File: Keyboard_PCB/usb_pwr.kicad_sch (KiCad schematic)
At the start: 57 parts, among them J2 USB-C 16P, U2 USBLC6-2SC6, U5 MCP73871, U6 MCP73871

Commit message: Battery charger layout done
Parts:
- removed C24: 22u, Capacitor_SMD:C_0603_1608Metric, symbol Device:C_Small
- removed C25: 100n, Capacitor_SMD:C_0603_1608Metric, symbol Device:C_Small
- removed C26, C27, C33, C34: 4u7, Capacitor_SMD:C_0603_1608Metric, symbol Device:C_Small
- removed C31, C32: 10u, Capacitor_SMD:C_0603_1608Metric, symbol Device:C_Small
- removed D5: PG, LED_SMD:LED_0603_1608Metric, symbol Device:LED_Small
- removed JP2: BAT_BYP, Jumper:SolderJumper-2_P1.3mm_Open_TrianglePad1.0x1.5mm, symbol Jumper:SolderJumper_2_Open
- removed R16, R17, R18, R19: 470, Resistor_SMD:R_0603_1608Metric, symbol Device:R_Small
- removed R20, R21: 10k, Resistor_SMD:R_0603_1608Metric, symbol Device:R_Small
- removed TP1, TP2: TestPoint, TestPoint:TestPoint_Pad_D1.0mm, symbol Connector:TestPoint
- removed U3, U4: ~, Marijn_KiCad:QFN_DSJ, symbol Marijn:TPS63020
- removed U5, U6: MCP73871, Package_DFN_QFN:QFN-20-1EP_4x4mm_P0.5mm_EP2.5x2.5mm, symbol Battery_Management:MCP73871
- added D11: PG, LED_SMD:LED_0603_1608Metric, symbol Device:LED_Small
- added D4, D5: BAT54C, Package_TO_SOT_SMD:SOT-23, symbol Diode:BAT54C
- added U2, U4: ISL91127IR, Package_DFN_QFN:QFN-20-1EP_4x4mm_P0.5mm_EP2.7x2.7mm_ThermalVias, symbol Marijn:ISL91127IR
- added U5, U6: MCP73833, Package_DFN_QFN:DFN-10-1EP_3x3mm_P0.5mm_EP1.58x2.35mm, symbol Battery_Management:MCP73833-xxx-MF
- C15: value 10u -> 22u
- C17: value 22u -> 10u
- C19: value 100n -> 22u
- C20, C21: value 10u -> 1u
- C22, C23: value 22u -> 1u
- L2, L3: value 1u5 -> 1u
- R10, R13: value 180k -> 470; LCSC (none) -> C23186
- R11, R9: value 1M -> 470; LCSC (none) -> C23186
- R12, R8: value 1M -> 10k; LCSC (none) -> C23186
- TH1, TH2: value Thermistor_NTC -> 10k
- renumbered U2 to U3
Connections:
- net APP_PG is gone; now on an unnamed net: R14.2
- net +3V3: now also C15.1, U2.15 (FB), U2.17 (VOUT), U2.18 (VOUT), U2.19 (VOUT), U2.20 (VOUT); no longer C17.1, C18.1, R8.1, R9.1
- net +5V: now also C20.1, C22.1, D11.2 (A), D4.2, D5.2, U5.1 (V_{DD}), U5.2 (V_{DD}), U6.1 (V_{DD}), U6.2 (V_{DD})
- net APP_THERM: now also U5.8 (THERM)
- net BKUP_THERM: now also U6.8 (THERM)
- net GND: now also R12.1, R8.1, U2.13 (SGND), U2.14 (SGND), U2.21 (EPAD), U2.3 (PGND), U4.13 (SGND), U4.14 (SGND), U4.21 (EPAD), U4.3 (PGND), U5.11 (EP), U5.5 (V_{SS}), U6.11 (EP), U6.5 (V_{SS}); no longer R10.2, R13.2
- net VBAT: now also C18.1, C19.1, U4.15 (FB), U4.17 (VOUT), U4.18 (VOUT), U4.19 (VOUT), U4.20 (VOUT); no longer C22.1, C23.1, R11.1, R12.1
- net at D7.1 (K): now also R10.2
- net at R15.1: now also U6.7 (~{PG}); no longer D6.1 (K)
- net at R13.1: now also U6.3 (STAT1); no longer R11.2
- net at L3.2: now also U4.1 (LX2), U4.2 (LX2)
- net at L3.1: now also U4.4 (LX1), U4.5 (LX1)
- net APP_BAT: now reaches BT1.1 (+)
- net APP_BAT: now also C21.1, D4.1, U5.10 (V_{BAT}), U5.9 (V_{BAT})
- net BKUP_BAT: now reaches BT2.1 (+)
- net BKUP_BAT: now also C23.1, D5.1, U6.10 (V_{BAT}), U6.9 (V_{BAT})
- net at D8.1 (K): now also R11.2
- net at L2.1: now also U2.4 (LX1), U2.5 (LX1)
- net at L2.2: now also U2.1 (LX2), U2.2 (LX2)
- net at R14.1: now also U6.4 (STAT2)
- net at R10.1: now also U5.4 (STAT2); no longer R8.2
- net at D9.1 (K): now also R13.2
- net APP_STAT1: no longer names the net of R15.2
- net APP_STAT1: now also D11.1 (K)
- net PG0: no longer names the net of R9.2
- net PG0: now also D6.1 (K)
- net PG1 renamed BKUP_PROG
- net BKUP_PROG: now also U6.6 (PROG)
- removed net VIN: C20.1, C21.1
- net V_IN renamed PVIN
- net PVIN: now also C17.1, D4.3, D5.3, U2.10 (VIN), U2.11 (EN), U2.12 (MODE), U2.6 (PVIN), U2.7 (PVIN), U2.8 (PVIN), U2.9 (PVIN), U4.10 (VIN), U4.11 (EN), U4.12 (MODE), U4.6 (PVIN), U4.7 (PVIN), U4.8 (PVIN), U4.9 (PVIN); no longer C15.1
- new net: R9.1, U5.3 (STAT1)
- new net: R11.1, U5.7 (~{PG})
- new net APP_PROG: R8.2, U5.6 (PROG)
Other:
- note added: "100mA"
- note removed: "CLOSE TO BAT"

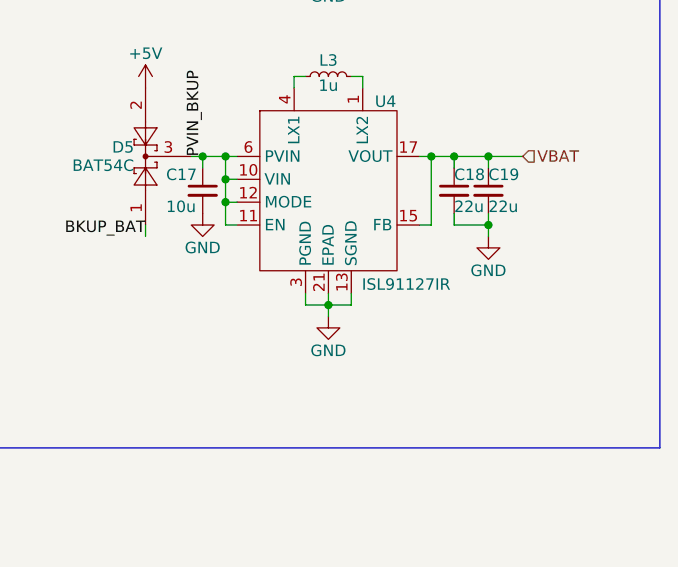
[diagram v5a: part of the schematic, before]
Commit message: Buck layout progress
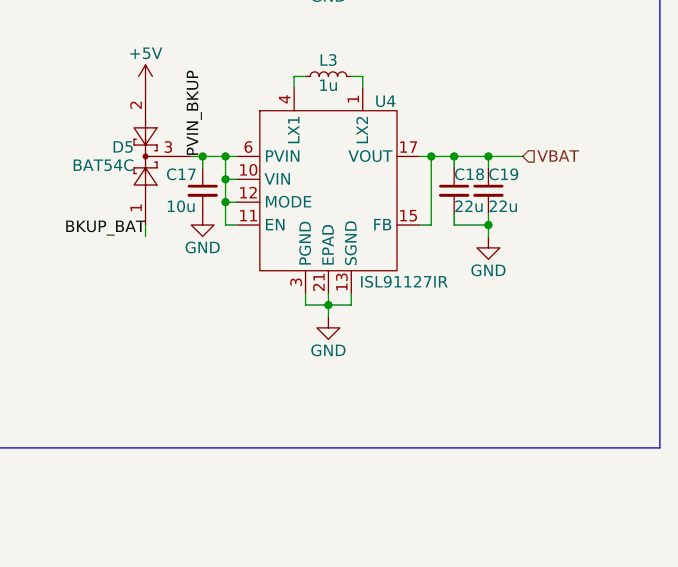
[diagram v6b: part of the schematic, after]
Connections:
- net PVIN renamed PVIN_APP
- net PVIN_APP: no longer C17.1, D5.3, U4.10 (VIN), U4.11 (EN), U4.12 (MODE), U4.6 (PVIN), U4.7 (PVIN), U4.8 (PVIN), U4.9 (PVIN)
- new net PVIN_BKUP: C17.1, D5.3, U4.10 (VIN), U4.11 (EN), U4.12 (MODE), U4.6 (PVIN), U4.7 (PVIN), U4.8 (PVIN), U4.9 (PVIN)
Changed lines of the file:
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@@
 	)
 	(symbol
+		(lib_id "Marijn:ISL91127IR")
+		(at 147.32 73.66 0)
+		(unit 1)
+		(exclude_from_sim no)
+		(in_bom yes)
+		(on_board yes)
+		(dnp no)
+		(property "Reference" "U4"
+			(at 153.67 66.294 0)
+			(effects
+				(font
+					(size 1.27 1.27)
+				)
+			)
+		)
+		(property "Value" "ISL91127IR"
+			(at 155.702 86.36 0)
+			(effects
+				(font
+					(size 1.27 1.27)
+				)
+			)
+		)
+		(property "Footprint" "Package_DFN_QFN:QFN-20-1EP_4x4mm_P0.5mm_EP2.7x2.7mm_ThermalVias"
+			(at 154.432 51.562 0)
+			(effects
+				(font
+					(size 1.27 1.27)
+				)
+				(hide yes)
+			)
+		)
+		(property "Datasheet" "https://nl.mouser.com/datasheet/2/698/REN_isl91127ir_DST_20220826-1998485.pdf"
+			(at 147.066 53.848 0)
+			(effects
+				(font
+					(size 1.27 1.27)
+				)
+				(hide yes)
+			)
+		)
+		(property "Description" ""
+			(at 147.32 73.66 0)
+			(effects
+				(font
+					(size 1.27 1.27)
+				)
+				(hide yes)
+			)
+		)
+		(pin "19"
+		)
+		(pin "18"
+		)
+		(pin "5"
+		)
+		(pin "2"
+		)
+		(pin "20"
+		)
+		(pin "21"
+		)
+		(pin "8"
+		)
+		(pin "9"
+		)
+		(pin "4"
+		)
+		(pin "7"
+		)
+		(pin "6"
+		)
+		(pin "3"
+		)
+		(pin "1"
+		)
+		(pin "10"
+		)
+		(pin "11"
+		)
+		(pin "12"
+		)
+		(pin "17"
+		)
+		(pin "13"
+		)
+		(pin "14"
+		)
+		(pin "15"
+		)
+		(instances
+			(project "Keyboard_PCB"
+				(path "/dd51e792-c76c-4d43-96de-494177f3b593/f183b390-0c59-4c65-8a55-408064b389c7"
+					(reference "U4")
+					(unit 1)
+				)
+			)
+		)
+	)
+	(symbol
 		(lib_id "power:+5V")
 		(at 67.31 33.02 0)
@@
 	)
 	(symbol
-		(lib_id "Marijn:ISL91127IR")
-		(at 147.32 34.29 0)
-		(unit 1)
-		(exclude_from_sim no)
-		(in_bom yes)
-		(on_board yes)
-		(dnp no)
-		(property "Reference" "U2"
-			(at 153.67 26.924 0)
-			(effects
-				(font
-					(size 1.27 1.27)
-				)
-			)
-		)
-		(property "Value" "ISL91127IR"
-			(at 155.702 46.99 0)
-			(effects
-				(font
-					(size 1.27 1.27)
-				)
-			)
-		)
-		(property "Footprint" "Package_DFN_QFN:QFN-20-1EP_4x4mm_P0.5mm_EP2.7x2.7mm_ThermalVias"
-			(at 154.432 12.192 0)
-			(effects
-				(font
-					(size 1.27 1.27)
-				)
-				(hide yes)
-			)
-		)
-		(property "Datasheet" "https://nl.mouser.com/datasheet/2/698/REN_isl91127ir_DST_20220826-1998485.pdf"
-			(at 147.066 14.478 0)
-			(effects
-				(font
-					(size 1.27 1.27)
-				)
-				(hide yes)
-			)
-		)
-		(property "Description" ""
-			(at 147.32 34.29 0)
-			(effects
-				(font
-					(size 1.27 1.27)
-				)
-				(hide yes)
-			)
-		)
-		(pin "3"
-		)
-		(pin "19"
-		)
-		(pin "9"
-		)
-		(pin "6"
-		)
-		(pin "13"
-		)
-		(pin "8"
-		)
-		(pin "10"
-		)
-		(pin "20"
-		)
-		(pin "17"
-		)
-		(pin "4"
-		)
-		(pin "7"
-		)
-		(pin "11"
-		)
-		(pin "2"
-		)
-		(pin "1"
-		)
-		(pin "5"
-		)
-		(pin "14"
-		)
-		(pin "15"
-		)
-		(pin "12"
-		)
-		(pin "18"
-		)
-		(pin "21"
-		)
-		(instances
-			(project ""
-				(path "/dd51e792-c76c-4d43-96de-494177f3b593/f183b390-0c59-4c65-8a55-408064b389c7"
-					(reference "U2")
-					(unit 1)
-				)
-			)
-		)
-	)
-	(symbol
 		(lib_id "Power_Protection:USBLC6-2SC6")
 		(at 67.31 38.1 0)
@@
 	)
 	(symbol
+		(lib_id "Marijn:ISL91127IR")
+		(at 147.32 34.29 0)
+		(unit 1)
+		(exclude_from_sim no)
+		(in_bom yes)
+		(on_board yes)
+		(dnp no)
+		(property "Reference" "U2"
+			(at 153.67 26.924 0)
+			(effects
+				(font
+					(size 1.27 1.27)
+				)
+			)
+		)
+		(property "Value" "ISL91127IR"
+			(at 155.702 46.99 0)
+			(effects
+				(font
+					(size 1.27 1.27)
+				)
+			)
+		)
+		(property "Footprint" "Package_DFN_QFN:QFN-20-1EP_4x4mm_P0.5mm_EP2.7x2.7mm_ThermalVias"
+			(at 154.432 12.192 0)
+			(effects
+				(font
+					(size 1.27 1.27)
+				)
+				(hide yes)
+			)
+		)
+		(property "Datasheet" "https://nl.mouser.com/datasheet/2/698/REN_isl91127ir_DST_20220826-1998485.pdf"
+			(at 147.066 14.478 0)
+			(effects
+				(font
+					(size 1.27 1.27)
+				)
+				(hide yes)
+			)
+		)
+		(property "Description" ""
+			(at 147.32 34.29 0)
+			(effects
+				(font
+					(size 1.27 1.27)
+				)
+				(hide yes)
+			)
+		)
+		(pin "19"
+		)
+		(pin "18"
+		)
+		(pin "5"
+		)
+		(pin "2"
+		)
+		(pin "20"
+		)
+		(pin "21"
+		)
+		(pin "8"
+		)
+		(pin "9"
+		)
+		(pin "4"
+		)
+		(pin "7"
+		)
+		(pin "6"
+		)
+		(pin "3"
+		)
+		(pin "1"
+		)
+		(pin "10"
+		)
+		(pin "11"
+		)
+		(pin "12"
+		)
+		(pin "17"
+		)
+		(pin "13"
+		)
+		(pin "14"
+		)
+		(pin "15"
+		)
+		(instances
+			(project ""
+				(path "/dd51e792-c76c-4d43-96de-494177f3b593/f183b390-0c59-4c65-8a55-408064b389c7"
+					(reference "U2")
+					(unit 1)
+				)
+			)
+		)
+	)
+	(symbol
 		(lib_id "power:GND")
 		(at 62.23 185.42 0)
@@
 					(unit 1)
 				)
-			)
-		)
-	)
-	(symbol
-		(lib_id "Marijn:ISL91127IR")
-		(at 147.32 73.66 0)
-		(unit 1)
-		(exclude_from_sim no)
-		(in_bom yes)
-		(on_board yes)
-		(dnp no)
-		(property "Reference" "U4"
-			(at 153.67 66.294 0)
-			(effects
-				(font
-					(size 1.27 1.27)
-				)
-			)
-		)
-		(property "Value" "ISL91127IR"
-			(at 155.956 86.614 0)
-			(effects
-				(font
-					(size 1.27 1.27)
-				)
-			)
-		)
-		(property "Footprint" "Package_DFN_QFN:QFN-20-1EP_4x4mm_P0.5mm_EP2.7x2.7mm_ThermalVias"
-			(at 154.432 51.562 0)
-			(effects
-				(font
-					(size 1.27 1.27)
-				)
-				(hide yes)
-			)
-		)
-		(property "Datasheet" "https://nl.mouser.com/datasheet/2/698/REN_isl91127ir_DST_20220826-1998485.pdf"
-			(at 147.066 53.848 0)
-			(effects
-				(font
-					(size 1.27 1.27)
-				)
-				(hide yes)
-			)
-		)
-		(property "Description" ""
-			(at 147.32 73.66 0)
-			(effects
-				(font
-					(size 1.27 1.27)
-				)
-				(hide yes)
-			)
-		)
-		(pin "3"
-		)
-		(pin "19"
-		)
-		(pin "9"
-		)
-		(pin "6"
-		)
-		(pin "13"
-		)
-		(pin "8"
-		)
-		(pin "10"
-		)
-		(pin "20"
-		)
-		(pin "17"
-		)
-		(pin "4"
-		)
-		(pin "7"
-		)
-		(pin "11"
-		)
-		(pin "2"
-		)
-		(pin "1"
-		)
-		(pin "5"
-		)
-		(pin "14"
-		)
-		(pin "15"
-		)
-		(pin "12"
-		)
-		(pin "18"
-		)
-		(pin "21"
-		)
-		(instances
-			(project "Keyboard_PCB"
-				(path "/dd51e792-c76c-4d43-96de-494177f3b593/f183b390-0c59-4c65-8a55-408064b389c7"
-					(reference "U4")
-					(unit 1)
-				)

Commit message: Power section finished
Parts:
- added TP1: 5V, symbol Connector:TestPoint
- added TP2: 3V3, symbol Connector:TestPoint
- added TP3: Vbat, symbol Connector:TestPoint
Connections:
- net +3V3: now also TP2.1
- net +5V: now also TP1.1
- net VBAT: now also TP3.1
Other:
- moved on the sheet: D3, F1, FL1, J2, R7, U3

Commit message: Layout V1
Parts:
- TP1: footprint (none) -> TestPoint:TestPoint_Pad_D2.0mm
- TP2, TP3: footprint (none) -> TestPoint:TestPoint_Pad_D1.5mm
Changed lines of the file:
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@@
 			)
 		)
-		(property "Footprint" ""
+		(property "Footprint" "TestPoint:TestPoint_Pad_D1.5mm"
 			(at 170.18 72.39 0)
 			(effects
@@
 			)
 		)
-		(property "Footprint" ""
+		(property "Footprint" "TestPoint:TestPoint_Pad_D2.0mm"
 			(at 55.88 27.94 0)
 			(effects
@@
 			)
 		)
-		(property "Footprint" ""
+		(property "Footprint" "TestPoint:TestPoint_Pad_D1.5mm"
 			(at 168.91 38.1 0)
 			(effects
